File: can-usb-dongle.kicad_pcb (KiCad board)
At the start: 2 copper layers, 30 x 15 mm, 43 parts, among them SW1 SW_PUSH, U1 STM32F302C8T, U2 SN65HVD256, U3 NUF2042XV6, U4 MCP1700, U5 SiP32431, X1 16MHz 10ppm

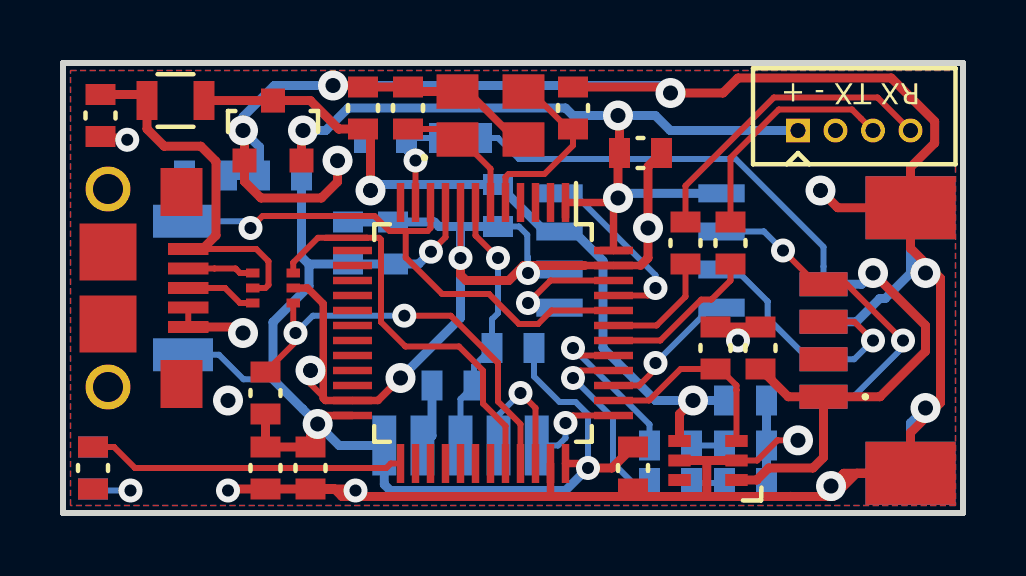
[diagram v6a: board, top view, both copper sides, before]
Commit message: Change USB footprint back to slot version
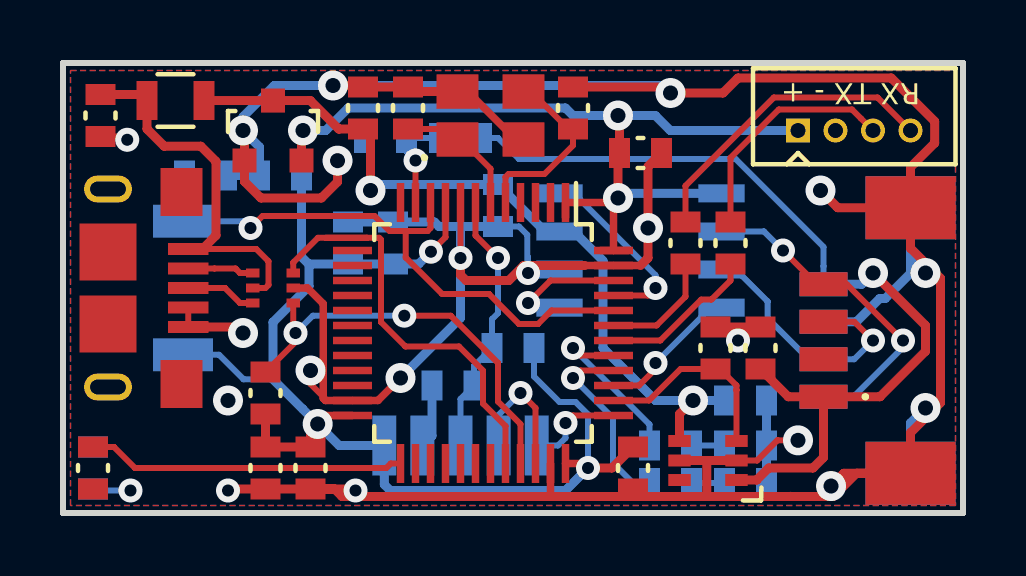
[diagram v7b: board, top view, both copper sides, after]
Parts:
- CONN3: footprint _connectors:_Micro-USB-AB-receptacle-SMT-th-no-slot -> _connectors:_Micro-USB-AB-receptacle-SMT-th
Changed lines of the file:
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@@
 (kicad_pcb (version 4) (host pcbnew "(2015-10-14 BZR 6267)-product")
   (general
-    (links 0)
+    (links 115)
     (no_connects 6)
-    (area 44.899999 37.399999 75.100001 52.600001)
+    (area 25.087299 28.495199 91.421702 60.2)
     (thickness 1.6)
     (drawings 22)
@@
     (pad 4 thru_hole circle (at 3.75 0) (size 0.8 0.8) (drill 0.5) (layers *.Cu *.Mask)
       (net 29 "Net-(CONN1-Pad4)"))
-  )
-  (module _connectors:_Micro-USB-AB-receptacle-SMT-th-no-slot (layer F.Cu)
-    (at 46.5 45 270)
-    (descr "part number: 10118193-0001LF")
-    (tags "micro USB, connector, receptacle")
-    (fp_text reference CONN3 (at 0 -5.5 270) (layer F.SilkS) hide
-      (effects (font (size 0.5 0.5) (thickness 0.125)))
-    )
-    (fp_text value MICRO_USB (at 0 -4.5 270) (layer F.SilkS) hide
-      (effects (font (size 0.5 0.5) (thickness 0.125)))
-    )
-    (pad 6 smd rect (at 1.2 0 270) (size 1.9 1.9) (layers F.Cu F.Mask)
-      (net 10 "Net-(CONN3-Pad6)") (solder_mask_margin 0.2) (clearance 0.3))
-    (pad 6 smd rect (at -1.2 0 270) (size 1.9 1.9) (layers F.Cu F.Mask)
-      (net 10 "Net-(CONN3-Pad6)") (solder_mask_margin 0.2) (clearance 0.3))
-    (pad 6 smd rect (at -3.2 -2.45 270) (size 1.6 1.4) (layers F.Cu F.Mask)
-      (net 10 "Net-(CONN3-Pad6)") (solder_mask_margin 0.2) (clearance 0.3))
-    (pad 6 smd rect (at 3.2 -2.45 270) (size 1.6 1.4) (layers F.Cu F.Mask)
-      (net 10 "Net-(CONN3-Pad6)") (solder_mask_margin 0.2) (clearance 0.3))
-    (pad 1 smd rect (at -1.3 -2.675 270) (size 0.4 1.35) (layers F.Cu F.Mask)
-      (net 7 "Net-(C13-Pad1)") (solder_mask_margin 0.15) (clearance 0.24))
-    (pad 2 smd rect (at -0.65 -2.675 270) (size 0.4 1.35) (layers F.Cu F.Mask)
-      (net 22 "Net-(CONN3-Pad2)") (solder_mask_margin 0.15) (clearance 0.24))
-    (pad 5 smd rect (at 1.3 -2.675 270) (size 0.4 1.35) (layers F.Cu F.Mask)
-      (net 2 GND) (solder_mask_margin 0.15) (clearance 0.24))
-    (pad 4 smd rect (at 0.65 -2.675 270) (size 0.4 1.35) (layers F.Cu F.Mask)
-      (net 2 GND) (solder_mask_margin 0.15) (clearance 0.24))
-    (pad 3 smd rect (at 0 -2.675 270) (size 0.4 1.35) (layers F.Cu F.Mask)
-      (net 23 "Net-(CONN3-Pad3)") (solder_mask_margin 0.15) (clearance 0.24))
-    (pad 6 thru_hole circle (at 3.3 0 270) (size 1.5 1.5) (drill 1) (layers *.Cu *.Mask F.SilkS)
-      (net 10 "Net-(CONN3-Pad6)") (solder_mask_margin 0.2) (clearance 0.3))
-    (pad 6 thru_hole circle (at -3.3 0 270) (size 1.5 1.5) (drill 1) (layers *.Cu *.Mask F.SilkS)
-      (net 10 "Net-(CONN3-Pad6)") (solder_mask_margin 0.2) (clearance 0.3))
   )
   (module _logo:CVRA-logo-small (layer B.Cu)
@@
       (xy -0.7874 1.563219) (xy -0.751417 1.572684) (xy 0.002117 1.572684) (xy 0.095991 1.572681)) (layer B.SilkS) (width 0.01))
   )
+  (module _connectors:_Micro-USB-AB-receptacle-SMT-th (layer F.Cu)
+    (at 46.5 45 270)
+    (descr "part number: 10118193-0001LF")
+    (tags "micro USB, connector, receptacle")
+    (fp_text reference CONN3 (at 0 -5.5 270) (layer F.SilkS) hide
+      (effects (font (size 0.5 0.5) (thickness 0.125)))
+    )
+    (fp_text value MICRO_USB (at 0 -4.5 270) (layer F.SilkS) hide
+      (effects (font (size 0.5 0.5) (thickness 0.125)))
+    )
+    (pad 6 smd rect (at 1.2 0 270) (size 1.9 1.9) (layers F.Cu F.Mask)
+      (net 10 "Net-(CONN3-Pad6)") (solder_mask_margin 0.2) (clearance 0.3))
+    (pad 6 smd rect (at -1.2 0 270) (size 1.9 1.9) (layers F.Cu F.Mask)
+      (net 10 "Net-(CONN3-Pad6)") (solder_mask_margin 0.2) (clearance 0.3))
+    (pad 6 smd rect (at -3.2 -2.45 270) (size 1.6 1.4) (layers F.Cu F.Mask)
+      (net 10 "Net-(CONN3-Pad6)") (solder_mask_margin 0.2) (clearance 0.3))
+    (pad 6 smd rect (at 3.2 -2.45 270) (size 1.6 1.4) (layers F.Cu F.Mask)
+      (net 10 "Net-(CONN3-Pad6)") (solder_mask_margin 0.2) (clearance 0.3))
+    (pad 1 smd rect (at -1.3 -2.675 270) (size 0.4 1.35) (layers F.Cu F.Mask)
+      (net 7 "Net-(C13-Pad1)") (solder_mask_margin 0.15) (clearance 0.24))
+    (pad 2 smd rect (at -0.65 -2.675 270) (size 0.4 1.35) (layers F.Cu F.Mask)
+      (net 22 "Net-(CONN3-Pad2)") (solder_mask_margin 0.15) (clearance 0.24))
+    (pad 5 smd rect (at 1.3 -2.675 270) (size 0.4 1.35) (layers F.Cu F.Mask)
+      (net 2 GND) (solder_mask_margin 0.15) (clearance 0.24))
+    (pad 4 smd rect (at 0.65 -2.675 270) (size 0.4 1.35) (layers F.Cu F.Mask)
+      (net 2 GND) (solder_mask_margin 0.15) (clearance 0.24))
+    (pad 3 smd rect (at 0 -2.675 270) (size 0.4 1.35) (layers F.Cu F.Mask)
+      (net 23 "Net-(CONN3-Pad3)") (solder_mask_margin 0.15) (clearance 0.24))
+    (pad 6 thru_hole oval (at 3.3 0 270) (size 0.9 1.6) (drill oval 0.5 1.2) (layers *.Cu *.Mask)
+      (net 10 "Net-(CONN3-Pad6)") (solder_mask_margin 0.2) (clearance 0.3))
+    (pad 6 thru_hole oval (at -3.3 0 270) (size 0.9 1.6) (drill oval 0.5 1.2) (layers *.Cu *.Mask)
+      (net 10 "Net-(CONN3-Pad6)") (solder_mask_margin 0.2) (clearance 0.3))
+  )
   (gr_text CVRA (at 52.1 51.2 180) (layer B.SilkS)

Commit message: GND connection, tracks
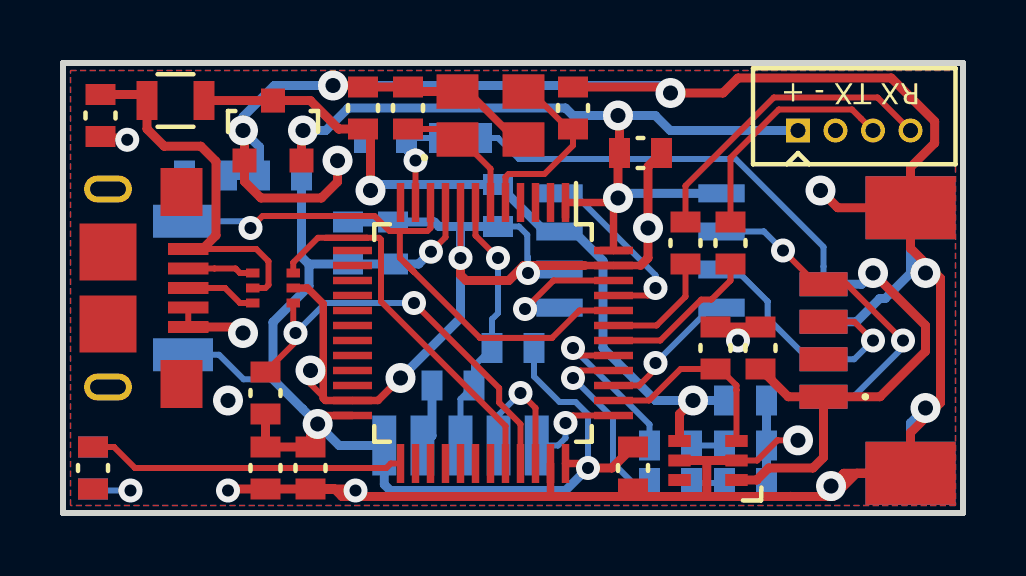
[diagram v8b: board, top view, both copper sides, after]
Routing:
- net /USB_D-: track 15.2 -> 14.2 mm
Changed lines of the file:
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@@
     (thickness 1.6)
     (drawings 22)
-    (tracks 477)
+    (tracks 470)
     (zones 0)
     (modules 43)
@@
   (segment (start 61.769981 50.869981) (end 61.75 50.85) (width 0.25) (layer F.Cu) (net 1))
   (via (at 62.5 51) (size 0.8) (drill 0.4) (layers F.Cu B.Cu) (net 1))
+  (segment (start 56.25 48) (end 58.25 46) (width 0.3) (layer B.Cu) (net 2))
+  (segment (start 58.25 46) (end 58.25 44) (width 0.3) (layer B.Cu) (net 2))
   (segment (start 68.25 46.3) (end 67.95 46.3) (width 0.2) (layer F.Cu) (net 2))
   (segment (start 67.95 46.3) (end 67.5 46.75) (width 0.2) (layer F.Cu) (net 2))
@@
   (segment (start 54.65 48.75) (end 55.5 48.75) (width 0.25) (layer F.Cu) (net 2))
   (segment (start 55.5 48.75) (end 56.25 48) (width 0.25) (layer F.Cu) (net 2))
-  (segment (start 56.25 48) (end 58.25 46) (width 0.3) (layer B.Cu) (net 2))
-  (segment (start 58.25 46) (end 58.25 44) (width 0.3) (layer B.Cu) (net 2))
   (via (at 56.25 48) (size 1) (drill 0.5) (layers F.Cu B.Cu) (net 2))
   (segment (start 50.45 41.25) (end 51.55 41.25) (width 0.3) (layer B.Cu) (net 2))
@@
   (segment (start 47.4 51) (end 55.775 51) (width 0.2) (layer F.Cu) (net 13))
   (segment (start 55.925 50.85) (end 56.25 50.85) (width 0.2) (layer F.Cu) (net 13))
+  (segment (start 56.229049 43.100001) (end 55.884999 43.100001) (width 0.2) (layer F.Cu) (net 14))
+  (segment (start 57.149999 43.100001) (end 56.229049 43.100001) (width 0.2) (layer F.Cu) (net 14))
+  (segment (start 58.900001 46.663999) (end 56.689849 44.453847) (width 0.2) (layer F.Cu) (net 14))
+  (segment (start 56.689849 44.453847) (end 56.4234 44.187398) (width 0.2) (layer F.Cu) (net 14))
+  (segment (start 56.229049 43.100001) (end 56.229049 43.993047) (width 0.2) (layer F.Cu) (net 14))
+  (segment (start 56.229049 43.993047) (end 56.689849 44.453847) (width 0.2) (layer F.Cu) (net 14))
+  (segment (start 63.35 45.75) (end 62.213998 45.75) (width 0.2) (layer F.Cu) (net 14))
+  (segment (start 62.213998 45.75) (end 61.299999 46.663999) (width 0.2) (layer F.Cu) (net 14))
+  (segment (start 61.299999 46.663999) (end 58.900001 46.663999) (width 0.2) (layer F.Cu) (net 14))
   (segment (start 49.05 41.25) (end 49.05 42.725) (width 0.2) (layer B.Cu) (net 14))
   (segment (start 49.05 42.725) (end 49 42.775) (width 0.2) (layer B.Cu) (net 14))
   (segment (start 49 42.775) (end 51.025 42.775) (width 0.2) (layer B.Cu) (net 14))
   (segment (start 51.025 42.775) (end 51.25 43) (width 0.2) (layer B.Cu) (net 14))
-  (segment (start 57.149999 43.100001) (end 55.884999 43.100001) (width 0.2) (layer F.Cu) (net 14))
   (segment (start 55.884999 43.100001) (end 55.384999 42.600001) (width 0.2) (layer F.Cu) (net 14))
   (segment (start 55.384999 42.600001) (end 51.649999 42.600001) (width 0.2) (layer F.Cu) (net 14))
@@
   (segment (start 57.149999 43.100001) (end 57.25 43) (width 0.2) (layer F.Cu) (net 14))
   (segment (start 57.25 43) (end 57.25 42.15) (width 0.2) (layer F.Cu) (net 14))
-  (segment (start 60.200001 46.200001) (end 59.200011 45.200011) (width 0.2) (layer F.Cu) (net 14))
-  (segment (start 57.638602 45.200011) (end 56.4234 43.984809) (width 0.2) (layer F.Cu) (net 14))
-  (segment (start 59.200011 45.200011) (end 57.638602 45.200011) (width 0.2) (layer F.Cu) (net 14))
-  (segment (start 56.4234 43.984809) (end 56.4234 43.100001) (width 0.2) (layer F.Cu) (net 14))
-  (segment (start 63.35 45.75) (end 61.286002 45.75) (width 0.2) (layer F.Cu) (net 14))
-  (segment (start 61.286002 45.75) (end 60.836001 46.200001) (width 0.2) (layer F.Cu) (net 14))
-  (segment (start 60.836001 46.200001) (end 60.200001 46.200001) (width 0.2) (layer F.Cu) (net 14))
   (via (at 51.25 43) (size 0.8) (drill 0.4) (layers F.Cu B.Cu) (net 14))
-  (segment (start 57.149999 43.100001) (end 56.4234 43.100001) (width 0.2) (layer F.Cu) (net 14))
-  (segment (start 56.565078 43.101132) (end 56.566209 43.100001) (width 0.2) (layer F.Cu) (net 14))
-  (segment (start 57.149999 43.100001) (end 56.566209 43.100001) (width 0.2) (layer F.Cu) (net 14))
   (segment (start 56.45 40) (end 57.55 40) (width 0.2) (layer B.Cu) (net 15))
   (segment (start 56.45 40) (end 56.45 40.45) (width 0.2) (layer B.Cu) (net 15))
@@
   (segment (start 56.75 42.15) (end 56.75 40.75) (width 0.2) (layer F.Cu) (net 15))
   (via (at 56.75 40.75) (size 0.8) (drill 0.4) (layers F.Cu B.Cu) (net 15))
-  (segment (start 56.376986 45.923025) (end 53.326975 45.923025) (width 0.2) (layer B.Cu) (net 16))
-  (segment (start 53.326975 45.923025) (end 52.75 46.5) (width 0.2) (layer B.Cu) (net 16))
-  (segment (start 56.376986 45.923025) (end 57.923025 45.923025) (width 0.2) (layer F.Cu) (net 16))
-  (segment (start 57.923025 45.923025) (end 59.5 47.5) (width 0.2) (layer F.Cu) (net 16))
-  (segment (start 59.5 47.5) (end 59.5 48.786002) (width 0.2) (layer F.Cu) (net 16))
-  (segment (start 59.5 48.786002) (end 60.25 49.536002) (width 0.2) (layer F.Cu) (net 16))
-  (segment (start 60.25 49.536002) (end 60.25 50.85) (width 0.2) (layer F.Cu) (net 16))
-  (via (at 56.376986 45.923025) (size 0.8) (drill 0.4) (layers F.Cu B.Cu) (net 16))
+  (segment (start 60.25 50.85) (end 60.25 49.536001) (width 0.2) (layer F.Cu) (net 16))
+  (segment (start 60.25 49.536001) (end 59.539899 48.8259) (width 0.2) (layer F.Cu) (net 16))
+  (segment (start 59.539899 48.8259) (end 59.539899 48.339899) (width 0.2) (layer F.Cu) (net 16))
+  (segment (start 59.539899 48.339899) (end 56.7 45.5) (width 0.2) (layer F.Cu) (net 16))
+  (segment (start 56.7 45.5) (end 53.75 45.5) (width 0.2) (layer B.Cu) (net 16))
+  (segment (start 53.75 45.5) (end 52.75 46.5) (width 0.2) (layer B.Cu) (net 16))
+  (via (at 56.7 45.5) (size 0.8) (drill 0.4) (layers F.Cu B.Cu) (net 16))
   (segment (start 52.75 46.5) (end 52.75 46.8) (width 0.2) (layer F.Cu) (net 16))
   (segment (start 52.75 46.8) (end 51.75 47.8) (width 0.2) (layer F.Cu) (net 16))
@@
   (segment (start 62.025 41.845) (end 64.75 44.57) (width 0.2) (layer B.Cu) (net 18))
   (via (at 64.75 45) (size 0.8) (drill 0.4) (layers F.Cu B.Cu) (net 18))
-  (segment (start 60.5 45.5) (end 61.395 45.5) (width 0.2) (layer B.Cu) (net 19))
-  (segment (start 61.395 45.5) (end 61.55 45.655) (width 0.2) (layer B.Cu) (net 19))
-  (segment (start 63.35 44.75) (end 61.25 44.75) (width 0.2) (layer F.Cu) (net 19))
-  (segment (start 61.25 44.75) (end 60.5 45.5) (width 0.2) (layer F.Cu) (net 19))
-  (via (at 60.5 45.5) (size 0.8) (drill 0.4) (layers F.Cu B.Cu) (net 19))
+  (segment (start 60.4 45.7) (end 61.35 44.75) (width 0.2) (layer F.Cu) (net 19))
+  (segment (start 61.35 44.75) (end 63.35 44.75) (width 0.2) (layer F.Cu) (net 19))
+  (segment (start 61.55 45.655) (end 60.445 45.655) (width 0.2) (layer B.Cu) (net 19))
+  (segment (start 60.445 45.655) (end 60.4 45.7) (width 0.2) (layer B.Cu) (net 19))
+  (via (at 60.4 45.7) (size 0.8) (drill 0.4) (layers F.Cu B.Cu) (net 19))
   (segment (start 65.75 45.286002) (end 65.75 44.2) (width 0.2) (layer F.Cu) (net 20))
   (segment (start 64.786002 46.25) (end 65.75 45.286002) (width 0.2) (layer F.Cu) (net 20))
@@
   (via (at 64.75 47.5) (size 0.8) (drill 0.4) (layers F.Cu B.Cu) (net 24))
   (segment (start 66.845 45.655) (end 66.95 45.655) (width 0.2) (layer B.Cu) (net 24))
-  (segment (start 59.75 50.85) (end 59.75 49.6017) (width 0.2) (layer F.Cu) (net 25))
-  (segment (start 59.75 49.6017) (end 59 48.8517) (width 0.2) (layer F.Cu) (net 25))
-  (segment (start 58.200001 46.950001) (end 56.413999 46.950001) (width 0.2) (layer F.Cu) (net 25))
-  (segment (start 59 48.8517) (end 59 47.75) (width 0.2) (layer F.Cu) (net 25))
-  (segment (start 59 47.75) (end 58.200001 46.950001) (width 0.2) (layer F.Cu) (net 25))
-  (segment (start 56.413999 46.950001) (end 55.600001 46.136003) (width 0.2) (layer F.Cu) (net 25))
-  (segment (start 55.600001 46.136003) (end 55.600001 43.384999) (width 0.2) (layer F.Cu) (net 25))
+  (segment (start 59.75 50.85) (end 59.75 49.601699) (width 0.2) (layer F.Cu) (net 25))
+  (segment (start 59.75 49.601699) (end 55.600001 45.4517) (width 0.2) (layer F.Cu) (net 25))
+  (segment (start 55.600001 45.4517) (end 55.600001 43.384999) (width 0.2) (layer F.Cu) (net 25))
   (segment (start 55.600001 43.384999) (end 55.540001 43.324999) (width 0.2) (layer F.Cu) (net 25))
   (segment (start 55.540001 43.324999) (end 55.137313 43.324999) (width 0.2) (layer F.Cu) (net 25))
